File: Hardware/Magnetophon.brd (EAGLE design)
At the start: 105 x 19 mm, 23 parts, among them U2 TL072_

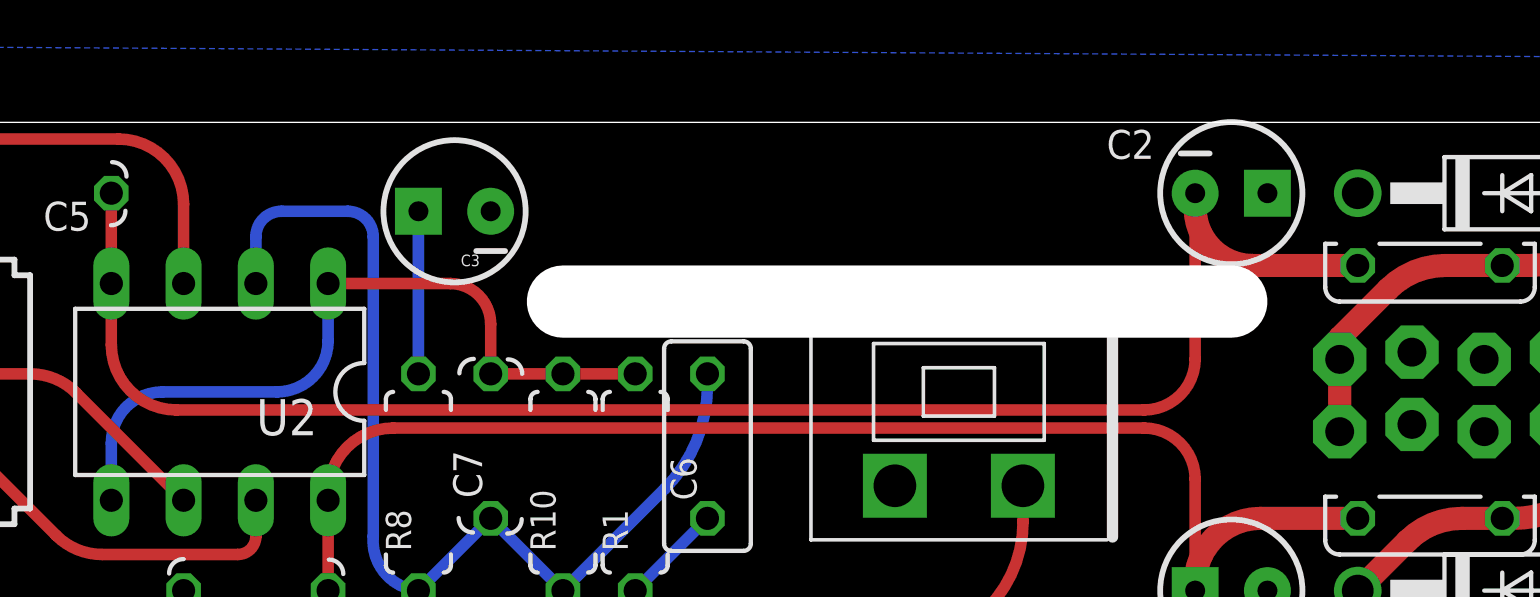
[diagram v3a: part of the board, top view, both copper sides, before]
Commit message: Fix issue with trace crossing cutout
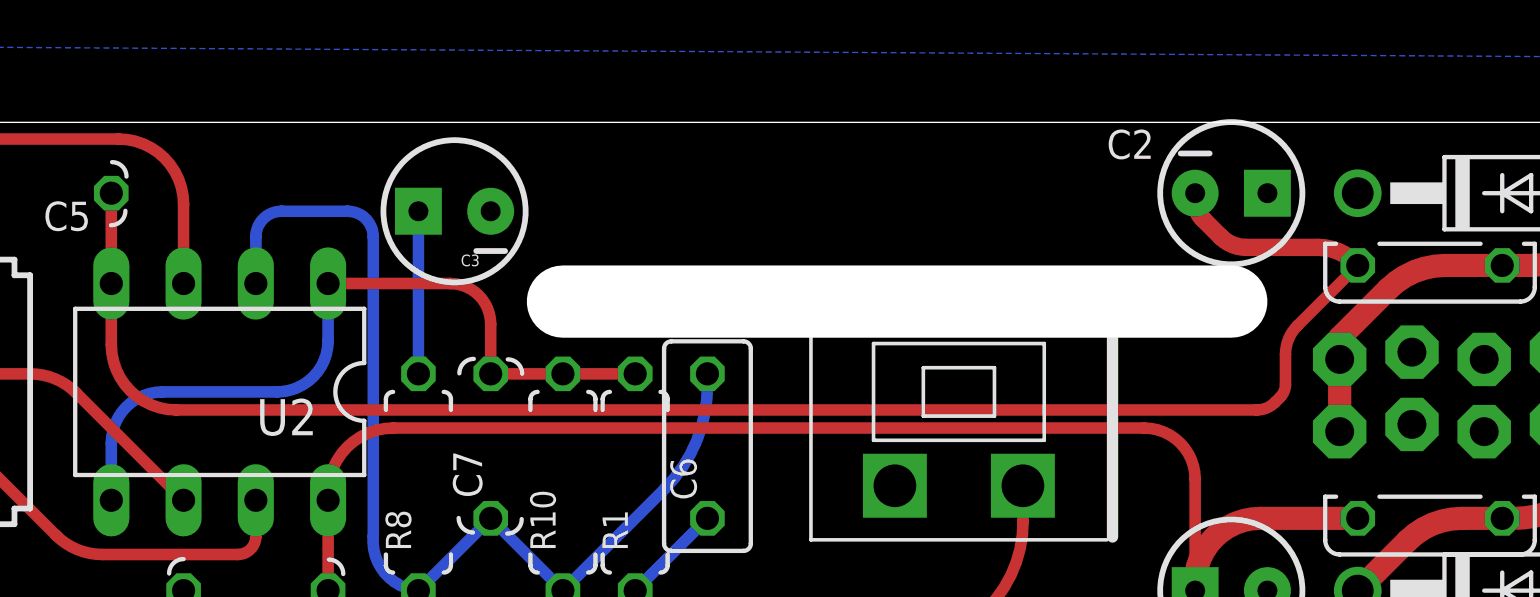
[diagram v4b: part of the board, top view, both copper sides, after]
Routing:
- net -12V: track 57.5 -> 60.0 mm
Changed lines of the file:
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@@
 <?xml version="1.0" encoding="utf-8"?>
 <!DOCTYPE eagle SYSTEM "eagle.dtd">
-<eagle version="7.2.0">
+<eagle version="7.4.0">
 <drawing>
 <settings>
@@
 <grid distance="25" unitdist="mil" unit="mil" style="lines" multiple="1" display="yes" altdistance="12.5" altunitdist="mil" altunit="mil"/>
 <layers>
-<layer number="1" name="Top" color="4" fill="1" visible="no" active="yes"/>
+<layer number="1" name="Top" color="4" fill="1" visible="yes" active="yes"/>
 <layer number="2" name="Route2" color="1" fill="3" visible="no" active="yes"/>
 <layer number="3" name="Route3" color="4" fill="3" visible="no" active="no"/>
@@
 <layer number="15" name="Route15" color="4" fill="6" visible="no" active="yes"/>
 <layer number="16" name="Bottom" color="1" fill="1" visible="yes" active="yes"/>
-<layer number="17" name="Pads" color="2" fill="1" visible="no" active="yes"/>
-<layer number="18" name="Vias" color="2" fill="1" visible="no" active="yes"/>
-<layer number="19" name="Unrouted" color="6" fill="1" visible="no" active="yes"/>
+<layer number="17" name="Pads" color="2" fill="1" visible="yes" active="yes"/>
+<layer number="18" name="Vias" color="2" fill="1" visible="yes" active="yes"/>
+<layer number="19" name="Unrouted" color="6" fill="1" visible="yes" active="yes"/>
 <layer number="20" name="Dimension" color="15" fill="1" visible="yes" active="yes"/>
 <layer number="21" name="tPlace" color="7" fill="1" visible="no" active="yes"/>
-<layer number="22" name="bPlace" color="7" fill="1" visible="yes" active="yes"/>
+<layer number="22" name="bPlace" color="7" fill="1" visible="no" active="yes"/>
 <layer number="23" name="tOrigins" color="15" fill="1" visible="no" active="yes"/>
-<layer number="24" name="bOrigins" color="15" fill="1" visible="yes" active="yes"/>
+<layer number="24" name="bOrigins" color="15" fill="1" visible="no" active="yes"/>
 <layer number="25" name="tNames" color="7" fill="1" visible="no" active="yes"/>
 <layer number="26" name="bNames" color="7" fill="1" visible="no" active="yes"/>
@@
 <layer number="28" name="bValues" color="7" fill="1" visible="no" active="yes"/>
 <layer number="29" name="tStop" color="7" fill="3" visible="no" active="yes"/>
-<layer number="30" name="bStop" color="7" fill="6" visible="yes" active="yes"/>
+<layer number="30" name="bStop" color="7" fill="6" visible="no" active="yes"/>
 <layer number="31" name="tCream" color="7" fill="4" visible="no" active="yes"/>
 <layer number="32" name="bCream" color="7" fill="5" visible="no" active="yes"/>
@@
 <layer number="39" name="tKeepout" color="4" fill="11" visible="no" active="yes"/>
 <layer number="40" name="bKeepout" color="1" fill="11" visible="no" active="yes"/>
-<layer number="41" name="tRestrict" color="4" fill="10" visible="no" active="yes"/>
-<layer number="42" name="bRestrict" color="1" fill="10" visible="no" active="yes"/>
+<layer number="41" name="tRestrict" color="4" fill="10" visible="yes" active="yes"/>
+<layer number="42" name="bRestrict" color="1" fill="10" visible="yes" active="yes"/>
 <layer number="43" name="vRestrict" color="2" fill="10" visible="no" active="yes"/>
 <layer number="44" name="Drills" color="7" fill="1" visible="no" active="yes"/>
 <layer number="45" name="Holes" color="7" fill="1" visible="no" active="yes"/>
-<layer number="46" name="Milling" color="3" fill="1" visible="no" active="yes"/>
+<layer number="46" name="Milling" color="3" fill="1" visible="yes" active="yes"/>
 <layer number="47" name="Measures" color="7" fill="1" visible="no" active="yes"/>
 <layer number="48" name="Document" color="7" fill="1" visible="no" active="yes"/>
@@
 <contactref element="U2" pad="4"/>
 <wire x1="49.53" y1="16.51" x2="49.53" y2="13.335" width="0.4064" layer="1"/>
-<wire x1="93.345" y1="13.97" x2="89.63804375" y2="13.97" width="0.8128" layer="1"/>
-<wire x1="89.63804375" y1="13.97" x2="87.63" y2="15.97804375" width="0.8128" layer="1" curve="-90"/>
-<wire x1="87.63" y1="15.97804375" x2="87.63" y2="16.51" width="0.8128" layer="1"/>
-<wire x1="87.63" y1="15.97804375" x2="87.63" y2="10.68605" width="0.4064" layer="1"/>
-<wire x1="87.63" y1="10.68605" x2="85.83395" y2="8.89" width="0.4064" layer="1" curve="-90"/>
-<wire x1="85.83395" y1="8.89" x2="51.819525" y2="8.89" width="0.4064" layer="1"/>
+<wire x1="51.819525" y1="8.89" x2="89.798025" y2="8.89" width="0.4064" layer="1"/>
+<wire x1="89.798025" y1="8.89" x2="90.433025" y2="9.153025" width="0.4064" layer="1" curve="45"/>
+<wire x1="90.433025" y1="9.153025" x2="90.6190125" y2="9.3390125" width="0.4064" layer="1"/>
+<wire x1="90.6190125" y1="9.3390125" x2="90.805" y2="9.788025" width="0.4064" layer="1" curve="45"/>
+<wire x1="90.805" y1="9.788025" x2="90.805" y2="10.84185625" width="0.4064" layer="1"/>
+<wire x1="90.805" y1="10.84185625" x2="91.22088125" y2="11.84588125" width="0.4064" layer="1" curve="-45.000089"/>
+<wire x1="91.22088125" y1="11.84588125" x2="93.345" y2="13.97" width="0.4064" layer="1"/>
 <wire x1="51.819525" y1="8.89" x2="49.53" y2="11.179525" width="0.4064" layer="1" curve="-90"/>
 <wire x1="49.53" y1="11.179525" x2="49.53" y2="13.335" width="0.4064" layer="1"/>
+<wire x1="87.63" y1="16.51" x2="87.63" y2="16.246975" width="0.6096" layer="1"/>
+<wire x1="87.63" y1="16.246975" x2="87.893025" y2="15.611975" width="0.6096" layer="1" curve="45"/>
+<wire x1="87.893025" y1="15.611975" x2="88.528025" y2="14.976975" width="0.6096" layer="1"/>
+<wire x1="88.528025" y1="14.976975" x2="89.42605" y2="14.605" width="0.6096" layer="1" curve="45"/>
+<wire x1="89.42605" y1="14.605" x2="91.966053125" y2="14.605" width="0.6096" layer="1"/>
+<wire x1="91.966053125" y1="14.605" x2="93.23605" y2="14.07895" width="0.6096" layer="1" curve="-44.99993"/>
+<wire x1="93.23605" y1="14.07895" x2="93.345" y2="13.97" width="0.6096" layer="1"/>
 </signal>
 <signal name="N$8">
